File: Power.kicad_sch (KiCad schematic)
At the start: 17 parts, among them J1 USB_C_Receptacle_USB2.0, J3 Conn_01x02, SW1 SW_DPST, U2 AP61201Z6-7 buck, U3 MAX1811

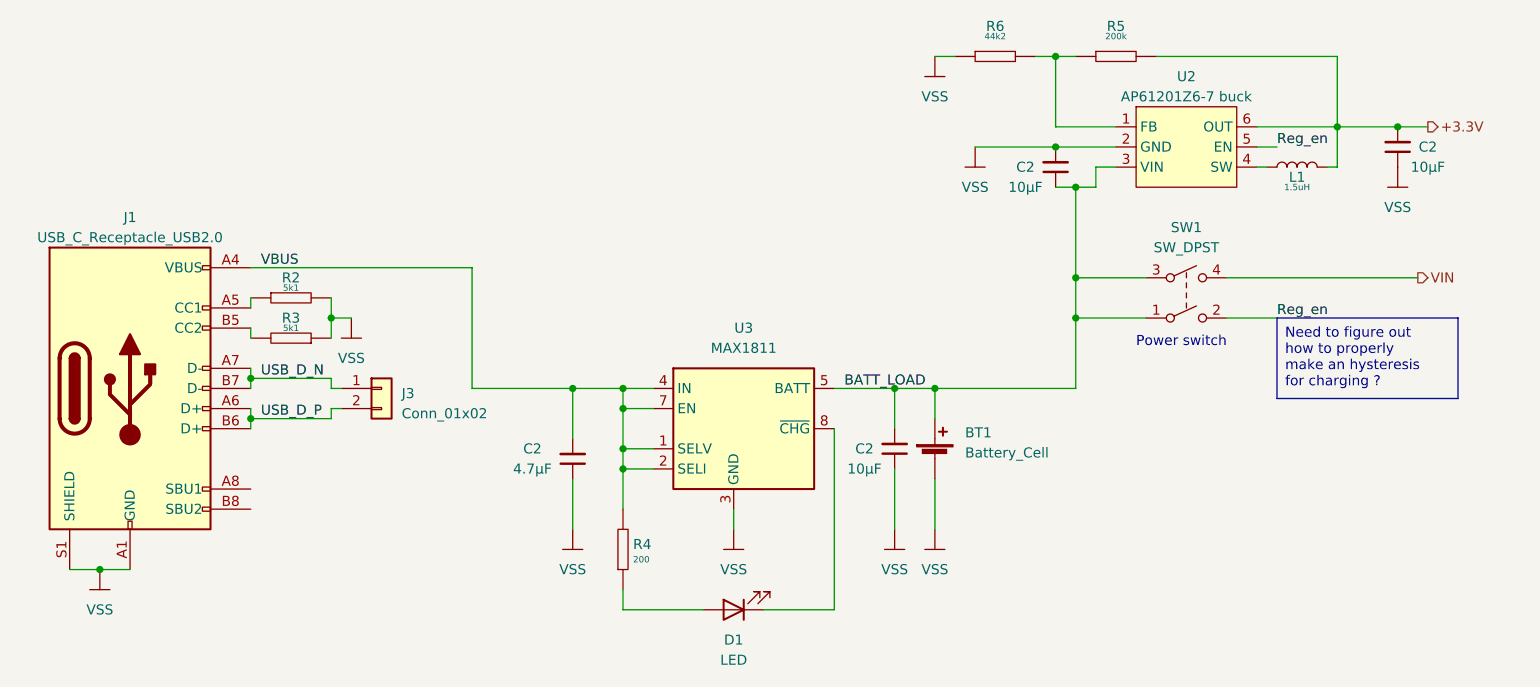
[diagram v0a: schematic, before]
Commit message: Améliorations après retour Victor
Allumage du régulateur maintenant géré par la teensy
Compaction de la carte pour rentrer sur 100x100mm
Ajout des trous de montage
Routage de la puissance du port USB maintenant sans boucle !
Un peu plus d'espace pour l'ampli'
Routage de l'ampli' avec des plans sur la sortie et une via par
condo pour l'entrée.
Moins de vias thermiques
Un seule via dans le pad de l'ampli'
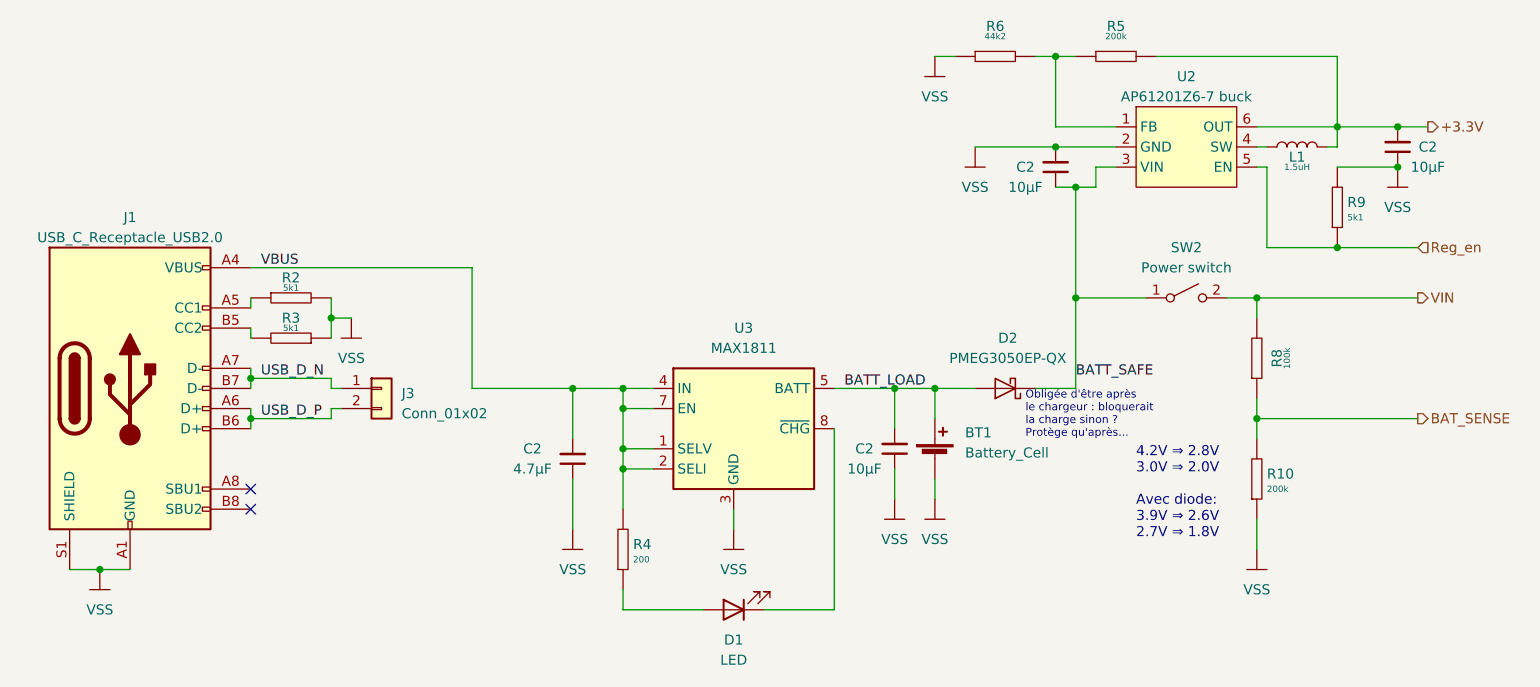
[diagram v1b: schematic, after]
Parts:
- removed SW1: SW_DPST, Connector_PinHeader_2.54mm:PinHeader_2x02_P2.54mm_Vertical, symbol Switch:SW_DPST
- added D2: PMEG3050EP-QX, Diode_SMD:D_SOD-128, symbol Diode:PMEG3020ER
- added R10: RES_0603_200k_1%, 01_Passives:RES_0603, symbol 02_Resistor:RES_0603_1K_1%
- added R8: RES_0603_100K_1%, 01_Passives:RES_0603, symbol 02_Resistor:RES_0603_10K_1%
- added R9: RES_0603_5K1_1%, 01_Passives:RES_0603, symbol 02_Resistor:RES_0603_2K1_1%
- added SW2: Power switch, Connector_PinHeader_2.54mm:PinHeader_1x02_P2.54mm_Vertical, symbol Switch:SW_SPST
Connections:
- net BATT_LOAD: now also D2.2 (A); no longer C2.1, U2.3 (VIN)
- net Reg_en: now also R9.1
- net VIN: now also R8.2, SW2.2 (B)
- net VSS: now also R10.1, R9.2
- new net BATT_SAFE: C2.1, D2.1 (K), SW2.1 (A), U2.3 (VIN)
- new net BAT_SENSE: R10.2, R8.1
- no-connect marks 0 -> 2
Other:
- note added: "4.2V ⇒ 2.8V 3.0V ⇒ 2.0V Avec diode: 3.9V ⇒ 2.6V 2.7V ⇒ 1.8V"
- note added: "Obligée d'être après le chargeur : bloquerait la charge sinon ? Protège qu'après..."
- note removed: "Power switch"
- moved on the sheet: L1

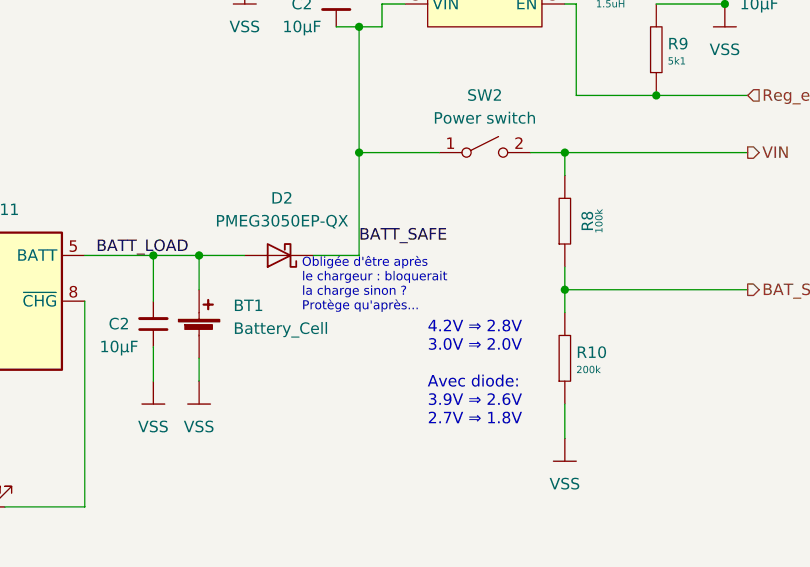
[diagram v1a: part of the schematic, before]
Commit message: Rev 0.3: Passage sur deux couches
Passage sur deux couches, ajustement de l'impédance pour l'USB.
Reroutage de l'alimentation côté USB
Ajout de beaucoup de silk
Quelques ajustements de nets pour la lisbilité
Ajout de LEDs de debug
Plan de masse sur le top
Quelques mises à jour sur le schematic
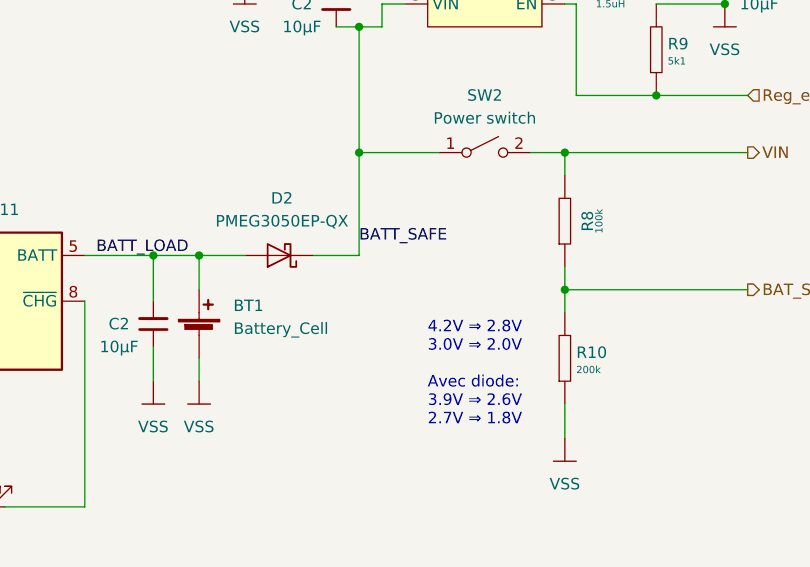
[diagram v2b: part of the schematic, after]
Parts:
- J3, SW2: now left out of the parts list
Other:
- note removed: "Obligée d'être après le chargeur : bloquerait la charge sinon ? Protège qu'après..."
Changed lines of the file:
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@@
   (title_block
     (title "Projet Barbapapa")
-    (date "2023-06-22")
-    (rev "0.2")
+    (date "2023-06-25")
+    (rev "0.3")
     (company "Téo-CD")
   )
@@
     (at 196.85 116.84 0)
     (effects (font (size 1.27 1.27)) (justify left bottom))
-  )
-  (text "Obligée d'être après\nle chargeur : bloquerait\nla charge sinon ?\nProtège qu'après..."
-    (at 182.88 104.14 0)
-    (effects (font (size 1 1)) (justify left bottom))
   )
   (label "USB_D_P" (at 86.36 101.6 0) (fields_autoplaced)
@@
   )
   (symbol (lib_id "Switch:SW_SPST") (at 203.2 86.36 0) (unit 1)
-    (in_bom yes) (on_board yes) (dnp no) (fields_autoplaced)
+    (in_bom no) (on_board yes) (dnp no) (fields_autoplaced)
     (property "Reference" "SW2" (at 203.2 80.01 0)
       (effects (font (size 1.27 1.27)))
@@
   )
   (symbol (lib_id "Connector_Generic:Conn_01x02") (at 101.6 97.79 0) (unit 1)
-    (in_bom yes) (on_board yes) (dnp no) (fields_autoplaced)
+    (in_bom no) (on_board yes) (dnp no) (fields_autoplaced)
     (property "Reference" "J3" (at 104.14 98.425 0)
       (effects (font (size 1.27 1.27)) (justify left))
